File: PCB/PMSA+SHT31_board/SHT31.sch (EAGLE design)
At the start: 8 parts, among them CN2 CON_PINHD-2X15, U2 SHT31-DIS

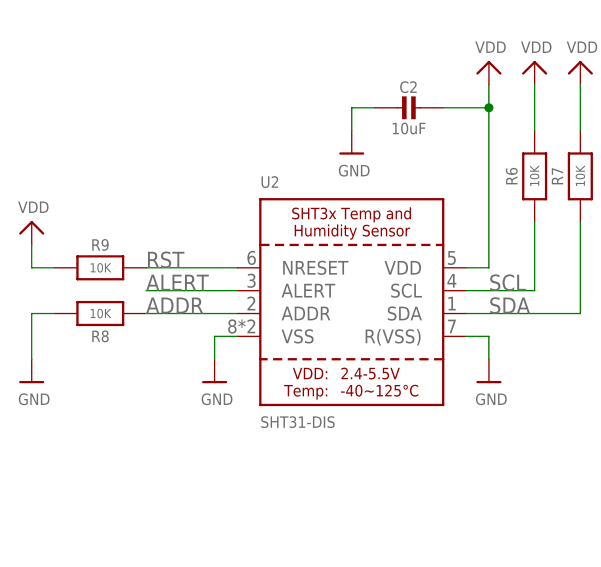
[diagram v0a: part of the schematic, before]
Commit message: insertion NOX & CO Captor
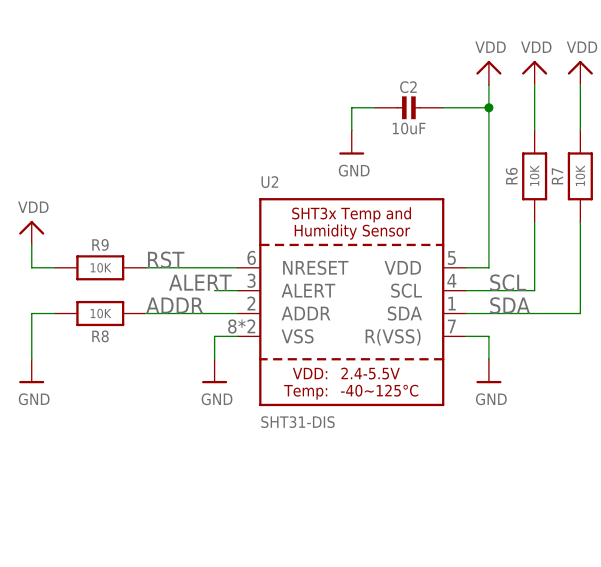
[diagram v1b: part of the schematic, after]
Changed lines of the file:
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@@
 <?xml version="1.0" encoding="utf-8"?>
 <!DOCTYPE eagle SYSTEM "eagle.dtd">
-<eagle version="9.3.2">
+<eagle version="9.4.2">
 <drawing>
 <settings>
@@
 <grid distance="0.1" unitdist="inch" unit="inch" style="lines" multiple="1" display="no" altdistance="0.01" altunitdist="inch" altunit="inch"/>
 <layers>
-<layer number="1" name="Top" color="4" fill="1" visible="yes" active="no"/>
-<layer number="2" name="Route2" color="16" fill="1" visible="yes" active="no"/>
-<layer number="3" name="Route3" color="17" fill="1" visible="yes" active="no"/>
-<layer number="4" name="Route4" color="18" fill="1" visible="yes" active="no"/>
-<layer number="5" name="Route5" color="19" fill="1" visible="yes" active="no"/>
-<layer number="6" name="Route6" color="25" fill="1" visible="yes" active="no"/>
-<layer number="7" name="Route7" color="26" fill="1" visible="yes" active="no"/>
-<layer number="8" name="Route8" color="27" fill="1" visible="yes" active="no"/>
-<layer number="9" name="Route9" color="28" fill="1" visible="yes" active="no"/>
-<layer number="10" name="Route10" color="29" fill="1" visible="yes" active="no"/>
-<layer number="11" name="Route11" color="30" fill="1" visible="yes" active="no"/>
-<layer number="12" name="Route12" color="20" fill="1" visible="yes" active="no"/>
-<layer number="13" name="Route13" color="21" fill="1" visible="yes" active="no"/>
-<layer number="14" name="Route14" color="22" fill="1" visible="yes" active="no"/>
-<layer number="15" name="Route15" color="23" fill="1" visible="yes" active="no"/>
-<layer number="16" name="Bottom" color="1" fill="1" visible="yes" active="no"/>
-<layer number="17" name="Pads" color="2" fill="1" visible="yes" active="no"/>
-<layer number="18" name="Vias" color="2" fill="1" visible="yes" active="no"/>
-<layer number="19" name="Unrouted" color="6" fill="1" visible="yes" active="no"/>
-<layer number="20" name="Dimension" color="24" fill="1" visible="yes" active="no"/>
-<layer number="21" name="tPlace" color="7" fill="1" visible="yes" active="no"/>
-<layer number="22" name="bPlace" color="7" fill="1" visible="yes" active="no"/>
-<layer number="23" name="tOrigins" color="15" fill="1" visible="yes" active="no"/>
-<layer number="24" name="bOrigins" color="15" fill="1" visible="yes" active="no"/>
-<layer number="25" name="tNames" color="7" fill="1" visible="yes" active="no"/>
-<layer number="26" name="bNames" color="7" fill="1" visible="yes" active="no"/>
-<layer number="27" name="tValues" color="7" fill="1" visible="yes" active="no"/>
-<layer number="28" name="bValues" color="7" fill="1" visible="yes" active="no"/>
+<layer number="1" name="Top" color="4" fill="1" visible="no" active="no"/>
+<layer number="2" name="Route2" color="16" fill="1" visible="no" active="no"/>
+<layer number="3" name="Route3" color="17" fill="1" visible="no" active="no"/>
+<layer number="4" name="Route4" color="18" fill="1" visible="no" active="no"/>
+<layer number="5" name="Route5" color="19" fill="1" visible="no" active="no"/>
+<layer number="6" name="Route6" color="25" fill="1" visible="no" active="no"/>
+<layer number="7" name="Route7" color="26" fill="1" visible="no" active="no"/>
+<layer number="8" name="Route8" color="27" fill="1" visible="no" active="no"/>
+<layer number="9" name="Route9" color="28" fill="1" visible="no" active="no"/>
+<layer number="10" name="Route10" color="29" fill="1" visible="no" active="no"/>
+<layer number="11" name="Route11" color="30" fill="1" visible="no" active="no"/>
+<layer number="12" name="Route12" color="20" fill="1" visible="no" active="no"/>
+<layer number="13" name="Route13" color="21" fill="1" visible="no" active="no"/>
+<layer number="14" name="Route14" color="22" fill="1" visible="no" active="no"/>
+<layer number="15" name="Route15" color="23" fill="1" visible="no" active="no"/>
+<layer number="16" name="Bottom" color="1" fill="1" visible="no" active="no"/>
+<layer number="17" name="Pads" color="2" fill="1" visible="no" active="no"/>
+<layer number="18" name="Vias" color="2" fill="1" visible="no" active="no"/>
+<layer number="19" name="Unrouted" color="6" fill="1" visible="no" active="no"/>
+<layer number="20" name="Dimension" color="24" fill="1" visible="no" active="no"/>
+<layer number="21" name="tPlace" color="7" fill="1" visible="no" active="no"/>
+<layer number="22" name="bPlace" color="7" fill="1" visible="no" active="no"/>
+<layer number="23" name="tOrigins" color="15" fill="1" visible="no" active="no"/>
+<layer number="24" name="bOrigins" color="15" fill="1" visible="no" active="no"/>
+<layer number="25" name="tNames" color="7" fill="1" visible="no" active="no"/>
+<layer number="26" name="bNames" color="7" fill="1" visible="no" active="no"/>
+<layer number="27" name="tValues" color="7" fill="1" visible="no" active="no"/>
+<layer number="28" name="bValues" color="7" fill="1" visible="no" active="no"/>
 <layer number="29" name="tStop" color="7" fill="3" visible="no" active="no"/>
 <layer number="30" name="bStop" color="7" fill="6" visible="no" active="no"/>
@@
 <layer number="35" name="tGlue" color="7" fill="4" visible="no" active="no"/>
 <layer number="36" name="bGlue" color="7" fill="5" visible="no" active="no"/>
-<layer number="37" name="tTest" color="7" fill="1" visible="yes" active="no"/>
-<layer number="38" name="bTest" color="7" fill="1" visible="yes" active="no"/>
+<layer number="37" name="tTest" color="7" fill="1" visible="no" active="no"/>
+<layer number="38" name="bTest" color="7" fill="1" visible="no" active="no"/>
 <layer number="39" name="tKeepout" color="4" fill="11" visible="no" active="no"/>
 <layer number="40" name="bKeepout" color="1" fill="11" visible="no" active="no"/>
@@
 <layer number="44" name="Drills" color="7" fill="1" visible="no" active="no"/>
 <layer number="45" name="Holes" color="7" fill="1" visible="no" active="no"/>
-<layer number="46" name="Milling" color="3" fill="1" visible="yes" active="no"/>
-<layer number="47" name="Measures" color="7" fill="1" visible="yes" active="no"/>
-<layer number="48" name="Document" color="7" fill="1" visible="yes" active="no"/>
-<layer number="49" name="Reference" color="7" fill="1" visible="yes" active="no"/>
-<layer number="50" name="dxf" color="7" fill="1" visible="yes" active="no"/>
-<layer number="51" name="tDocu" color="7" fill="1" visible="yes" active="no"/>
-<layer number="52" name="bDocu" color="7" fill="1" visible="yes" active="no"/>
-<layer number="53" name="tGND_GNDA" color="7" fill="9" visible="yes" active="no"/>
-<layer number="54" name="bGND_GNDA" color="1" fill="9" visible="yes" active="no"/>
-<layer number="56" name="wert" color="7" fill="1" visible="yes" active="no"/>
-<layer number="57" name="tCAD" color="7" fill="1" visible="yes" active="no"/>
-<layer number="58" name="b3D" color="7" fill="1" visible="yes" active="no"/>
-<layer number="59" name="Invisible" color="7" fill="1" visible="yes" active="no"/>
-<layer number="60" name="bCarbon" color="7" fill="1" visible="yes" active="no"/>
-<layer number="61" name="stand" color="7" fill="1" visible="yes" active="no"/>
+<layer number="46" name="Milling" color="3" fill="1" visible="no" active="no"/>
+<layer number="47" name="Measures" color="7" fill="1" visible="no" active="no"/>
+<layer number="48" name="Document" color="7" fill="1" visible="no" active="no"/>
+<layer number="49" name="Reference" color="7" fill="1" visible="no" active="no"/>
+<layer number="50" name="dxf" color="7" fill="1" visible="no" active="no"/>
+<layer number="51" name="tDocu" color="7" fill="1" visible="no" active="no"/>
+<layer number="52" name="bDocu" color="7" fill="1" visible="no" active="no"/>
+<layer number="53" name="tGND_GNDA" color="7" fill="9" visible="no" active="no"/>
+<layer number="54" name="bGND_GNDA" color="1" fill="9" visible="no" active="no"/>
+<layer number="56" name="wert" color="7" fill="1" visible="no" active="no"/>
+<layer number="57" name="tCAD" color="7" fill="1" visible="no" active="no"/>
+<layer number="58" name="b3D" color="7" fill="1" visible="no" active="no"/>
+<layer number="59" name="Invisible" color="7" fill="1" visible="no" active="no"/>
+<layer number="60" name="bCarbon" color="7" fill="1" visible="no" active="no"/>
+<layer number="61" name="stand" color="7" fill="1" visible="no" active="no"/>
 <layer number="88" name="SimResults" color="9" fill="1" visible="yes" active="yes"/>
 <layer number="89" name="SimProbes" color="9" fill="1" visible="yes" active="yes"/>
@@
 <segment>
 <pinref part="U2" gate="G$1" pin="ALERT"/>
-<wire x1="-147.32" y1="76.2" x2="-157.48" y2="76.2" width="0.1524" layer="91"/>
-<label x="-157.48" y="76.2" size="1.778" layer="95"/>
-</segment>
-</net>
+<wire x1="-147.32" y1="76.2" x2="-149.86" y2="76.2" width="0.1524" layer="91"/>
+<label x="-154.94" y="76.2" size="1.778" layer="95"/>
+</segment>
+</net>
